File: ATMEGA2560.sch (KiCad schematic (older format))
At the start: 22 parts, among them U1 ATmega2560-16AU

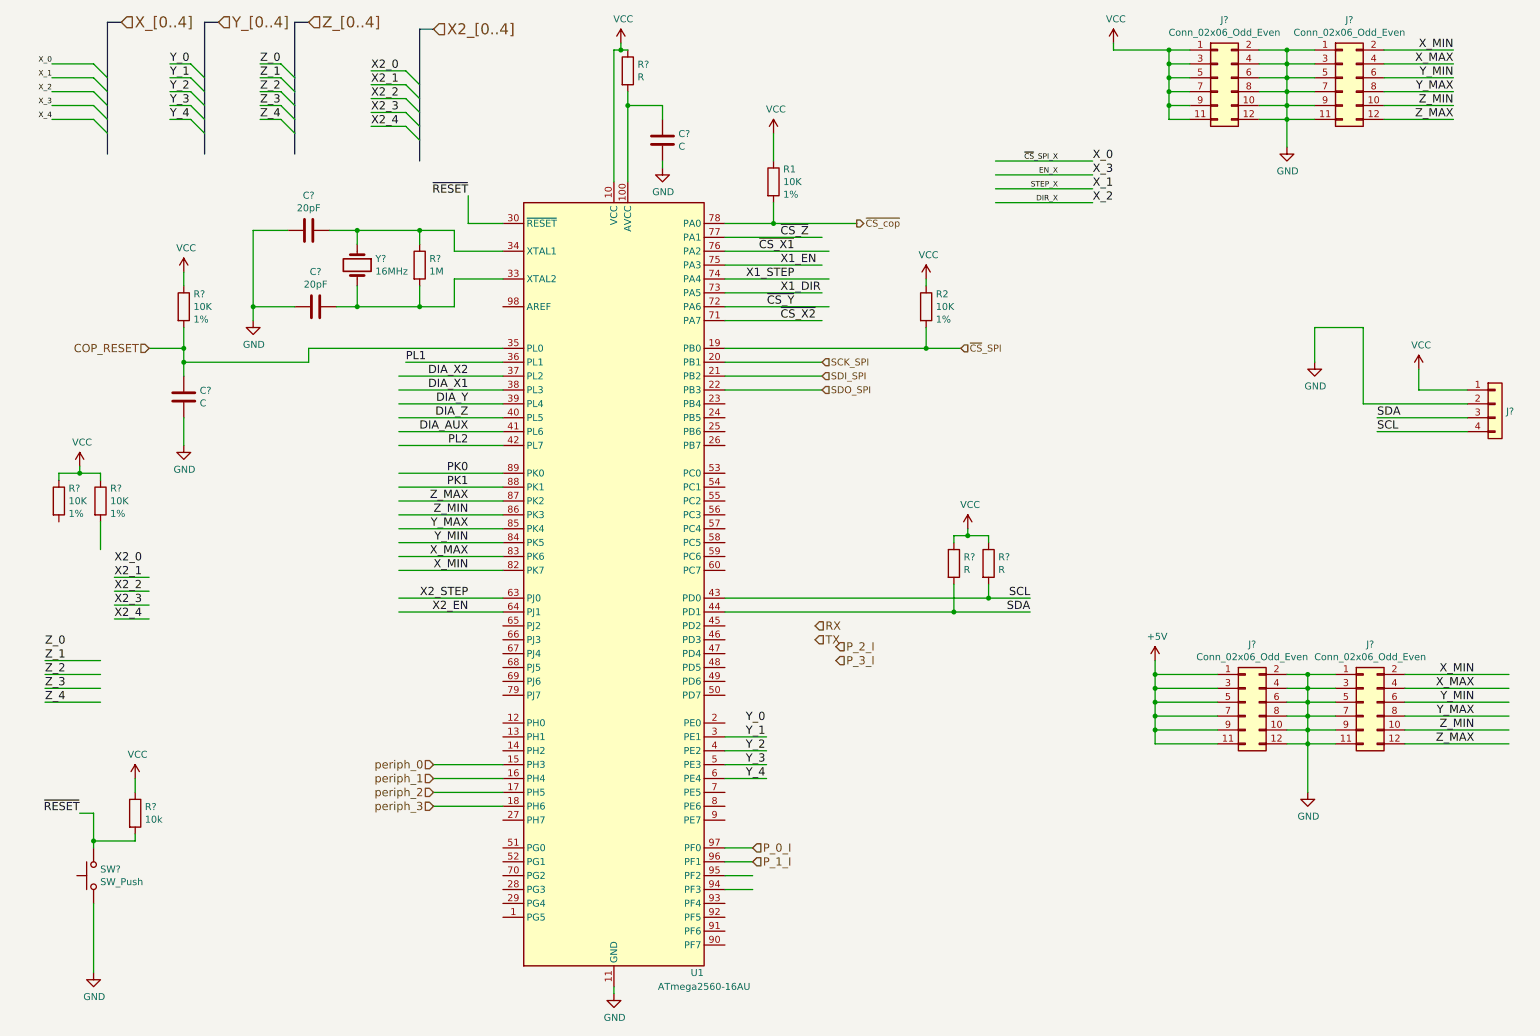
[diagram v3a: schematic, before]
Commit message: connected CoP + mP SPI. pushed updated into layout
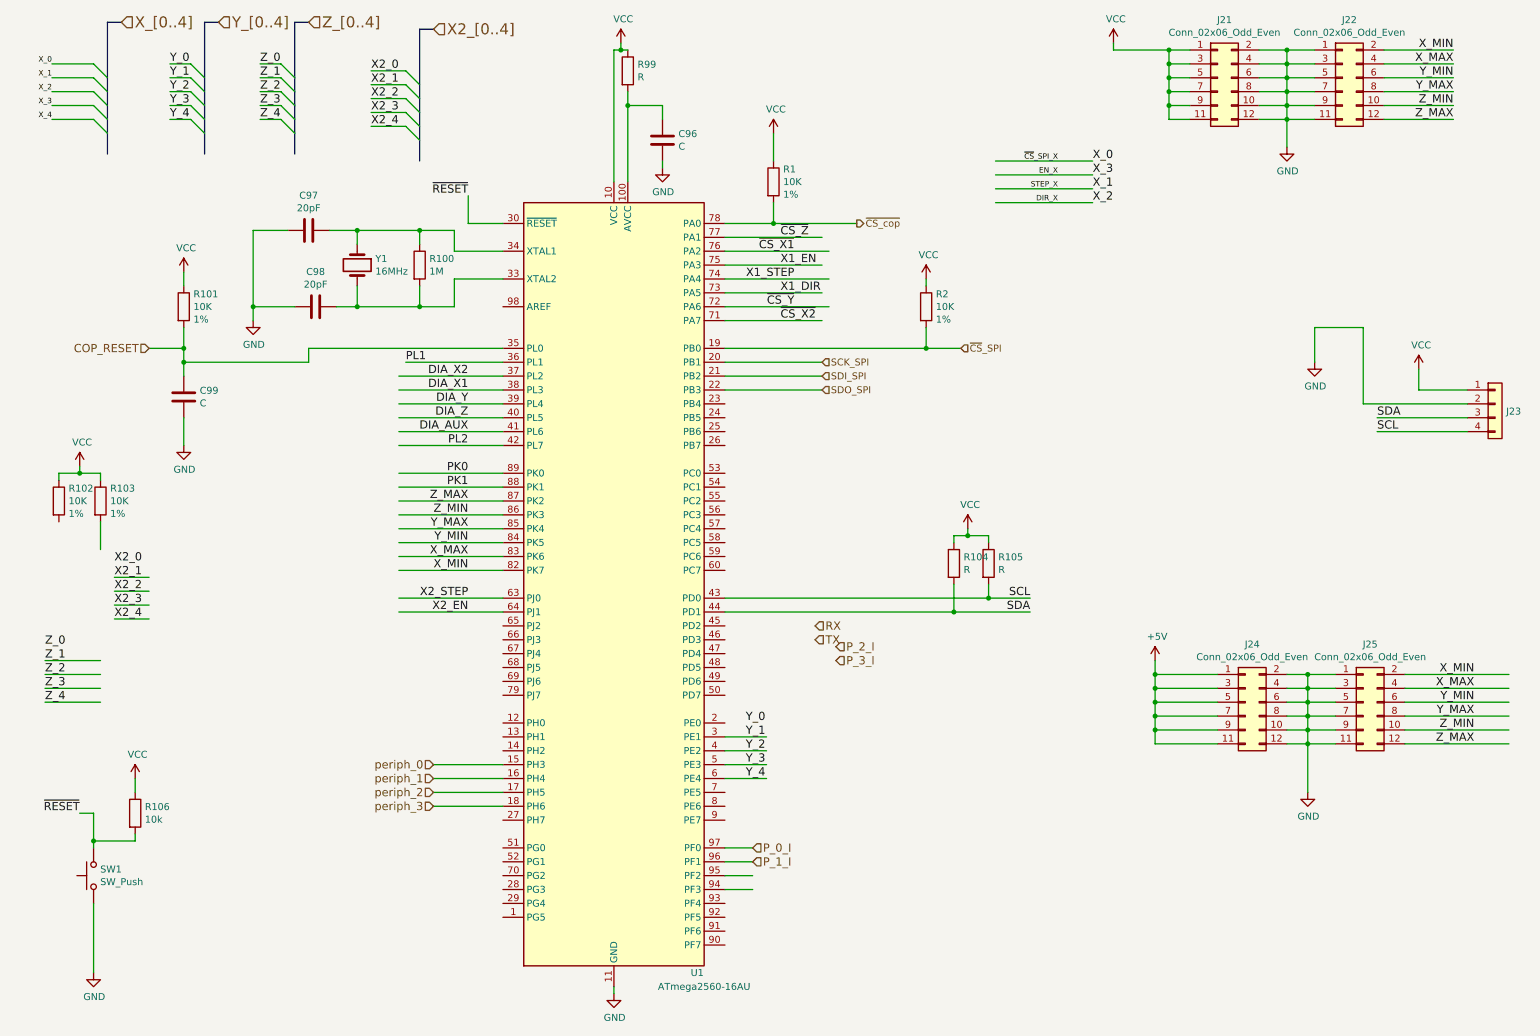
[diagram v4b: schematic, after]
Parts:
- gave numbers to parts that had none: 19
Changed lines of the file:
@@
 ~CS~_SPI_X
 $Comp
-L Device:Crystal Y?
+L Device:Crystal Y1
 U 1 1 61AB0536
 P 2800 2300
-F 0 "Y?" V 2754 2431 50  0000 L CNN
+F 0 "Y1" V 2754 2431 50  0000 L CNN
 F 1 "16MHz" V 2845 2431 50  0000 L CNN
 F 2 "Crystals:Crystal_HC49-4H_Vertical" H 2800 2300 50  0001 C CNN
@@
 	2800 2450 2800 2600
 $Comp
-L power:GND #PWR?
+L power:GND #PWR0262
 U 1 1 61AB97FE
 P 2050 2700
-F 0 "#PWR?" H 2050 2450 50  0001 C CNN
+F 0 "#PWR0262" H 2050 2450 50  0001 C CNN
 F 1 "GND" H 2055 2527 50  0000 C CNN
 F 2 "" H 2050 2700 50  0001 C CNN
@@
 	2050 2600 2050 2050
 $Comp
-L Device:C C?
+L Device:C C97
 U 1 1 61AC21F0
 P 2450 2050
-F 0 "C?" V 2198 2050 50  0000 C CNN
+F 0 "C97" V 2198 2050 50  0000 C CNN
 F 1 "20pF" V 2289 2050 50  0000 C CNN
 F 2 "Capacitors_SMD:C_0603_HandSoldering" H 2488 1900 50  0001 C CNN
@@
 	2650 2600 2800 2600
 $Comp
-L Device:R R?
+L Device:R R100
 U 1 1 61AC6E6D
 P 3250 2300
-F 0 "R?" H 3320 2346 50  0000 L CNN
+F 0 "R100" H 3320 2346 50  0000 L CNN
 F 1 "1M" H 3320 2255 50  0000 L CNN
 F 2 "Resistors_SMD:R_0805_HandSoldering" V 3180 2300 50  0001 C CNN
@@
 	3250 2600 3500 2600
 $Comp
-L Device:C C?
+L Device:C C98
 U 1 1 61ACDF29
 P 2500 2600
-F 0 "C?" V 2248 2600 50  0000 C CNN
+F 0 "C98" V 2248 2600 50  0000 C CNN
 F 1 "20pF" V 2339 2600 50  0000 C CNN
 F 2 "Capacitors_SMD:C_0603_HandSoldering" H 2538 2450 50  0001 C CNN
@@
 ~RESET
 $Comp
-L Switch:SW_Push SW?
+L Switch:SW_Push SW1
 U 1 1 61AD104B
 P 900 6700
-F 0 "SW?" V 946 6652 50  0000 R CNN
+F 0 "SW1" V 946 6652 50  0000 R CNN
 F 1 "SW_Push" V 855 6652 50  0000 R CNN
 F 2 "" H 900 6900 50  0001 C CNN
@@
 	900  6250 900  6450
 $Comp
-L power:GND #PWR?
+L power:GND #PWR0263
 U 1 1 61AD39B1
 P 900 7400
-F 0 "#PWR?" H 900 7150 50  0001 C CNN
+F 0 "#PWR0263" H 900 7150 50  0001 C CNN
 F 1 "GND" H 905 7227 50  0000 C CNN
 F 2 "" H 900 7400 50  0001 C CNN
@@
 	900  6450 900  6500
 $Comp
-L power:VCC #PWR?
+L power:VCC #PWR0264
 U 1 1 61ADE595
 P 4700 700
-F 0 "#PWR?" H 4700 550 50  0001 C CNN
+F 0 "#PWR0264" H 4700 550 50  0001 C CNN
 F 1 "VCC" H 4717 873 50  0000 C CNN
 F 2 "" H 4700 700 50  0001 C CNN
@@
 $EndComp
 $Comp
-L power:VCC #PWR?
+L power:VCC #PWR0265
 U 1 1 61ADE5C2
 P 1200 6000
-F 0 "#PWR?" H 1200 5850 50  0001 C CNN
+F 0 "#PWR0265" H 1200 5850 50  0001 C CNN
 F 1 "VCC" H 1217 6173 50  0000 C CNN
 F 2 "" H 1200 6000 50  0001 C CNN
@@
 AR Path="/5EEE69C6/61B1A8BA" Ref="R?"  Part="1"
 AR Path="/5FF92876/61B1A8BA" Ref="R?"  Part="1"
-AR Path="/5EE66603/61B1A8BA" Ref="R?"  Part="1"
-F 0 "R?" H 1270 6296 50  0000 L CNN
+AR Path="/5EE66603/61B1A8BA" Ref="R106"  Part="1"
+F 0 "R106" H 1270 6296 50  0000 L CNN
 F 1 "10k" H 1270 6205 50  0000 L CNN
 F 2 "Resistors_SMD:R_0603_HandSoldering" V 1130 6250 50  0001 C CNN
@@
 	3850 6200 3350 6200
 $Comp
-L power:VCC #PWR?
+L power:VCC #PWR0266
 U 1 1 6211D4EC
 P 5800 1350
-F 0 "#PWR?" H 5800 1200 50  0001 C CNN
+F 0 "#PWR0266" H 5800 1200 50  0001 C CNN
 F 1 "VCC" H 5817 1523 50  0000 C CNN
 F 2 "" H 5800 1350 50  0001 C CNN
@@
 	5800 1550 5800 1350
 $Comp
-L power:GND #PWR?
+L power:GND #PWR0267
 U 1 1 6212FBC9
 P 4650 7550
-F 0 "#PWR?" H 4650 7300 50  0001 C CNN
+F 0 "#PWR0267" H 4650 7300 50  0001 C CNN
 F 1 "GND" H 4655 7377 50  0000 C CNN
 F 2 "" H 4650 7550 50  0001 C CNN
@@
 	4650 7500 4650 7550
 $Comp
-L Device:R R?
+L Device:R R99
 U 1 1 62138ADE
 P 4750 900
-F 0 "R?" H 4820 946 50  0000 L CNN
+F 0 "R99" H 4820 946 50  0000 L CNN
 F 1 "R" H 4820 855 50  0000 L CNN
 F 2 "" V 4680 900 50  0001 C CNN
@@
 $EndComp
 $Comp
-L Device:C C?
+L Device:C C96
 U 1 1 62139E15
 P 5000 1400
-F 0 "C?" H 5115 1446 50  0000 L CNN
+F 0 "C96" H 5115 1446 50  0000 L CNN
 F 1 "C" H 5115 1355 50  0000 L CNN
 F 2 "" H 5038 1250 50  0001 C CNN
@@
 $EndComp
 $Comp
-L power:GND #PWR?
+L power:GND #PWR0268
 U 1 1 621486D7
 P 5000 1600
-F 0 "#PWR?" H 5000 1350 50  0001 C CNN
+F 0 "#PWR0268" H 5000 1350 50  0001 C CNN
 F 1 "GND" H 5005 1427 50  0000 C CNN
 F 2 "" H 5000 1600 50  0001 C CNN
@@
 	4750 1150 4750 1700
 $Comp
-L power:VCC #PWR?
+L power:VCC #PWR0269
 U 1 1 62170FDA
 P 6900 2400
-F 0 "#PWR?" H 6900 2250 50  0001 C CNN
+F 0 "#PWR0269" H 6900 2250 50  0001 C CNN
 F 1 "VCC" H 6917 2573 50  0000 C CNN
 F 2 "" H 6900 2400 50  0001 C CNN
@@
 	6900 2450 6900 2400
 $Comp
-L Device:R R?
+L Device:R R103
 U 1 1 6219C526
 P 950 4000
-F 0 "R?" H 1020 4091 50  0000 L CNN
+F 0 "R103" H 1020 4091 50  0000 L CNN
 F 1 "10K" H 1020 4000 50  0000 L CNN
 F 2 "" V 880 4000 50  0001 C CNN
@@
 $EndComp
 $Comp
-L Device:R R?
+L Device:R R102
 U 1 1 6219E013
 P 650 4000
-F 0 "R?" H 720 4091 50  0000 L CNN
+F 0 "R102" H 720 4091 50  0000 L CNN
 F 1 "10K" H 720 4000 50  0000 L CNN
 F 2 "" V 580 4000 50  0001 C CNN
@@
 $EndComp
 $Comp
-L power:VCC #PWR?
+L power:VCC #PWR0270
 U 1 1 621A8082
 P 800 3750
-F 0 "#PWR?" H 800 3600 50  0001 C CNN
+F 0 "#PWR0270" H 800 3600 50  0001 C CNN
 F 1 "VCC" H 817 3923 50  0000 C CNN
 F 2 "" H 800 3750 50  0001 C CNN
@@
 	5450 4800 7100 4800
 $Comp
-L Connector_Generic:Conn_02x06_Odd_Even J?
+L Connector_Generic:Conn_02x06_Odd_Even J21
 U 1 1 621F0167
 P 9000 950
-F 0 "J?" H 9050 1367 50  0000 C CNN
+F 0 "J21" H 9050 1367 50  0000 C CNN
 F 1 "Conn_02x06_Odd_Even" H 9050 1276 50  0000 C CNN
 F 2 "" H 9000 950 50  0001 C CNN
@@
 $EndComp
 $Comp
-L Connector_Generic:Conn_02x06_Odd_Even J?
+L Connector_Generic:Conn_02x06_Odd_Even J22
 U 1 1 621F1812
 P 9900 950
-F 0 "J?" H 9950 1367 50  0000 C CNN
+F 0 "J22" H 9950 1367 50  0000 C CNN
 F 1 "Conn_02x06_Odd_Even" H 9950 1276 50  0000 C CNN
 F 2 "" H 9900 950 50  0001 C CNN
@@
 	9700 1250 9500 1250
 $Comp
-L power:VCC #PWR?
+L power:VCC #PWR0271
 U 1 1 6220C0AC
 P 8250 700
-F 0 "#PWR?" H 8250 550 50  0001 C CNN
+F 0 "#PWR0271" H 8250 550 50  0001 C CNN
 F 1 "VCC" H 8267 873 50  0000 C CNN
 F 2 "" H 8250 700 50  0001 C CNN
@@
 Connection ~ 8650 750
 $Comp
-L power:GND #PWR?
+L power:GND #PWR0272
 U 1 1 62228741
 P 9500 1450
-F 0 "#PWR?" H 9500 1200 50  0001 C CNN
+F 0 "#PWR0272" H 9500 1200 50  0001 C CNN
 F 1 "GND" H 9505 1277 50  0000 C CNN
 F 2 "" H 9500 1450 50  0001 C CNN
@@
 Z_MIN
 $Comp
-L Connector_Generic:Conn_01x04 J?
+L Connector_Generic:Conn_01x04 J23
 U 1 1 6225576E
 P 11000 3300
-F 0 "J?" H 11080 3246 50  0000 L CNN
+F 0 "J23" H 11080 3246 50  0000 L CNN
 F 1 "Conn_01x04" H 11080 3201 50  0001 L CNN
 F 2 "" H 11000 3300 50  0001 C CNN
@@
 $EndComp
 $Comp
-L power:VCC #PWR?
+L power:VCC #PWR0273
 U 1 1 6225C489
 P 10450 3050
-F 0 "#PWR?" H 10450 2900 50  0001 C CNN
+F 0 "#PWR0273" H 10450 2900 50  0001 C CNN
 F 1 "VCC" H 10467 3223 50  0000 C CNN
 F 2 "" H 10450 3050 50  0001 C CNN
@@
 $EndComp
 $Comp
-L power:GND #PWR?
+L power:GND #PWR0274
 U 1 1 6225C82B
 P 9700 3000
-F 0 "#PWR?" H 9700 2750 50  0001 C CNN
+F 0 "#PWR0274" H 9700 2750 50  0001 C CNN
 F 1 "GND" H 9705 2827 50  0000 C CNN
 F 2 "" H 9700 3000 50  0001 C CNN
@@
 	9700 2750 9700 3000
 $Comp
-L Device:R R?
+L Device:R R104
 U 1 1 62287F3A
 P 7100 4450
-F 0 "R?" H 7170 4496 50  0000 L CNN
+F 0 "R104" H 7170 4496 50  0000 L CNN
 F 1 "R" H 7170 4405 50  0000 L CNN
 F 2 "" V 7030 4450 50  0001 C CNN
@@
 $EndComp
 $Comp
-L Device:R R?
+L Device:R R105
 U 1 1 62289125
 P 7350 4450
-F 0 "R?" H 7420 4496 50  0000 L CNN
+F 0 "R105" H 7420 4496 50  0000 L CNN
 F 1 "R" H 7420 4405 50  0000 L CNN
 F 2 "" V 7280 4450 50  0001 C CNN
@@
 	7350 4700 5450 4700
 $Comp
-L power:VCC #PWR?
+L power:VCC #PWR0275
 U 1 1 622AB8F4
 P 7200 4200
-F 0 "#PWR?" H 7200 4050 50  0001 C CNN
+F 0 "#PWR0275" H 7200 4050 50  0001 C CNN
 F 1 "VCC" H 7217 4373 50  0000 C CNN
 F 2 "" H 7200 4200 50  0001 C CNN
@@
 Connection ~ 6900 2900
 $Comp
-L Device:R R?
+L Device:R R101
 U 1 1 621EE858
 P 1550 2600
-F 0 "R?" H 1620 2691 50  0000 L CNN
+F 0 "R101" H 1620 2691 50  0000 L CNN
 F 1 "10K" H 1620 2600 50  0000 L CNN
 F 2 "" V 1480 2600 50  0001 C CNN
@@
 $EndComp
 $Comp
-L power:VCC #PWR?
+L power:VCC #PWR0276
 U 1 1 621EF1D2
 P 1550 2350
-F 0 "#PWR?" H 1550 2200 50  0001 C CNN
+F 0 "#PWR0276" H 1550 2200 50  0001 C CNN
 F 1 "VCC" H 1567 2523 50  0000 C CNN
 F 2 "" H 1550 2350 50  0001 C CNN
@@
 $EndComp
 $Comp
-L Device:C C?
+L Device:C C99
 U 1 1 621EF87D
 P 1550 3250
-F 0 "C?" H 1665 3296 50  0000 L CNN
+F 0 "C99" H 1665 3296 50  0000 L CNN
 F 1 "C" H 1665 3205 50  0000 L CNN
 F 2 "" H 1588 3100 50  0001 C CNN
@@
 	1550 2350 1550 2450
 $Comp
-L power:GND #PWR?
+L power:GND #PWR0277
 U 1 1 622083D2
 P 1550 3600
-F 0 "#PWR?" H 1550 3350 50  0001 C CNN
+F 0 "#PWR0277" H 1550 3350 50  0001 C CNN
 F 1 "GND" H 1555 3427 50  0000 C CNN
 F 2 "" H 1550 3600 50  0001 C CNN
@@
 	3100 4500 3850 4500
 $Comp
-L Connector_Generic:Conn_02x06_Odd_Even J?
+L Connector_Generic:Conn_02x06_Odd_Even J24
 U 1 1 62EF8F2F
 P 9200 5450
-F 0 "J?" H 9250 5867 50  0000 C CNN
+F 0 "J24" H 9250 5867 50  0000 C CNN
 F 1 "Conn_02x06_Odd_Even" H 9250 5776 50  0000 C CNN
 F 2 "" H 9200 5450 50  0001 C CNN
@@
 $EndComp
 $Comp
-L Connector_Generic:Conn_02x06_Odd_Even J?
+L Connector_Generic:Conn_02x06_Odd_Even J25
 U 1 1 62EF965D
 P 10050 5450
-F 0 "J?" H 10100 5867 50  0000 C CNN
+F 0 "J25" H 10100 5867 50  0000 C CNN
 F 1 "Conn_02x06_Odd_Even" H 10100 5776 50  0000 C CNN
 F 2 "" H 10050 5450 50  0001 C CNN
@@
 	10350 5250 11100 5250
 $Comp
-L power:GND #PWR?
+L power:GND #PWR0278
 U 1 1 62F30E7C
 P 9650 6100
-F 0 "#PWR?" H 9650 5850 50  0001 C CNN
+F 0 "#PWR0278" H 9650 5850 50  0001 C CNN
 F 1 "GND" H 9655 5927 50  0000 C CNN
 F 2 "" H 9650 6100 50  0001 C CNN
@@
 	9650 5750 9650 5650
 $Comp
-L power:+5V #PWR?
+L power:+5V #PWR0279
 U 1 1 62F81107
 P 8550 5150
-F 0 "#PWR?" H 8550 5000 50  0001 C CNN
+F 0 "#PWR0279" H 8550 5000 50  0001 C CNN
 F 1 "+5V" H 8565 5323 50  0000 C CNN
 F 2 "" H 8550 5150 50  0001 C CNN

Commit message: added footprints for most of the c,r, and tp's. need new buck
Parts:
- R1, R101, R102, R103, R2: footprint (none) -> Resistors_SMD:R_0603_HandSoldering
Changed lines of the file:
@@
 EESchema Schematic File Version 4
-EELAYER 30 0
+LIBS:bountifulHarvest-cache
+EELAYER 26 0
 EELAYER END
 $Descr A4 11693 8268
@@
 F 0 "R1" H 5870 1791 50  0000 L CNN
 F 1 "10K" H 5870 1700 50  0000 L CNN
-F 2 "" V 5730 1700 50  0001 C CNN
+F 2 "Resistors_SMD:R_0603_HandSoldering" V 5730 1700 50  0001 C CNN
 F 3 "~" H 5800 1700 50  0001 C CNN
 F 4 "1%" H 5870 1609 50  0000 L CNN "Tolerance"
@@
 F 0 "R2" H 6970 2691 50  0000 L CNN
 F 1 "10K" H 6970 2600 50  0000 L CNN
-F 2 "" V 6830 2600 50  0001 C CNN
+F 2 "Resistors_SMD:R_0603_HandSoldering" V 6830 2600 50  0001 C CNN
 F 3 "~" H 6900 2600 50  0001 C CNN
 F 4 "1%" H 6970 2509 50  0000 L CNN "Tolerance"
@@
 F 0 "R103" H 1020 4091 50  0000 L CNN
 F 1 "10K" H 1020 4000 50  0000 L CNN
-F 2 "" V 880 4000 50  0001 C CNN
+F 2 "Resistors_SMD:R_0603_HandSoldering" V 880 4000 50  0001 C CNN
 F 3 "~" H 950 4000 50  0001 C CNN
 F 4 "1%" H 1020 3909 50  0000 L CNN "Tolerance"
@@
 F 0 "R102" H 720 4091 50  0000 L CNN
 F 1 "10K" H 720 4000 50  0000 L CNN
-F 2 "" V 580 4000 50  0001 C CNN
+F 2 "Resistors_SMD:R_0603_HandSoldering" V 580 4000 50  0001 C CNN
 F 3 "~" H 650 4000 50  0001 C CNN
 F 4 "1%" H 720 3909 50  0000 L CNN "Tolerance"
@@
 F 0 "R101" H 1620 2691 50  0000 L CNN
 F 1 "10K" H 1620 2600 50  0000 L CNN
-F 2 "" V 1480 2600 50  0001 C CNN
+F 2 "Resistors_SMD:R_0603_HandSoldering" V 1480 2600 50  0001 C CNN
 F 3 "~" H 1550 2600 50  0001 C CNN
 F 4 "1%" H 1620 2509 50  0000 L CNN "Tolerance"
